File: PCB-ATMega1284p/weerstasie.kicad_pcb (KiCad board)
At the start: 2 copper layers, 35 x 87 mm, 42 parts, among them J1 WIND, J10 Conn_01x01, J11 INT2, J12 I2C, J13 UART, J2 batt -, J3 batt +, J4 RAIN, J5 Conn_01x01, J6 Conn_01x01, J7 Conn_01x01, J8 Conn_01x01, J9 Conn_01x01, SW1 SW_Push, U1 BME280, U2 RFM95, U3 ATMEGA1284P-AU, Y1 8MHz

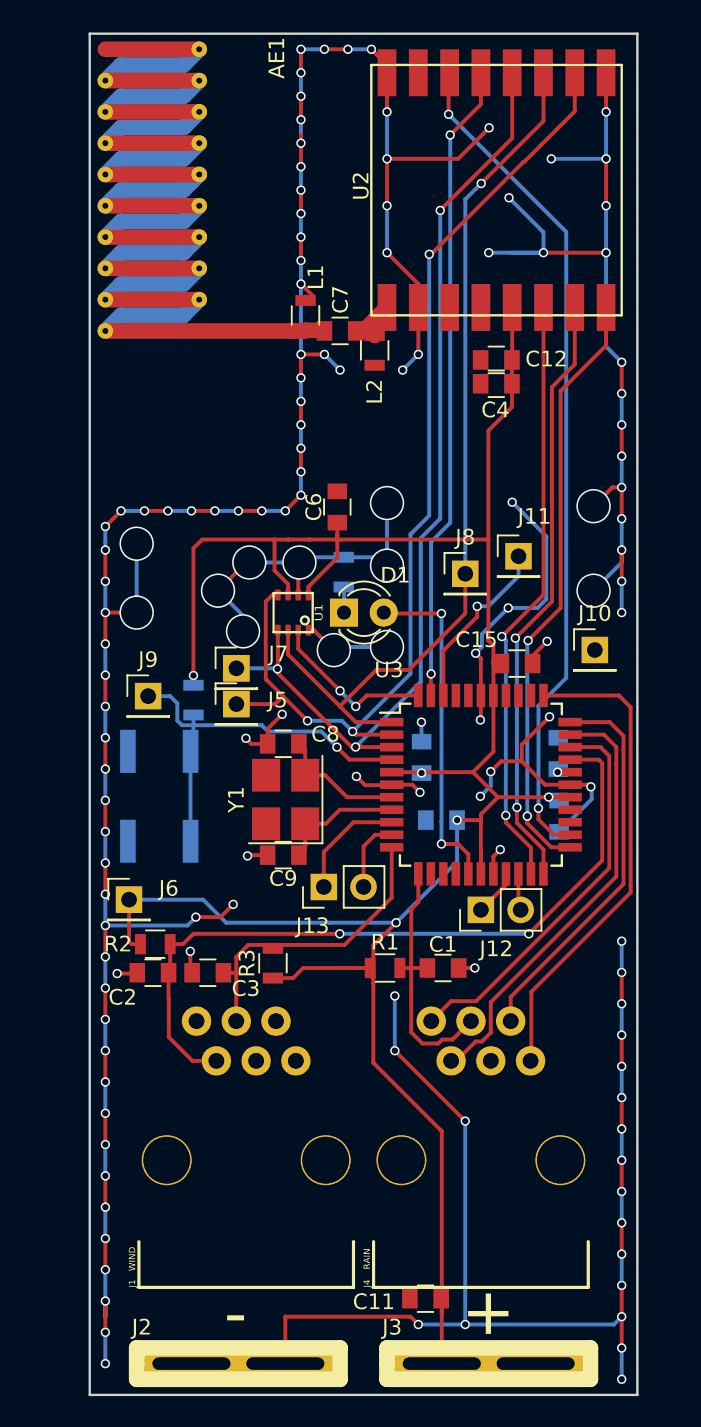
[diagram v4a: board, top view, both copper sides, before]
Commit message: Update to kicad 5 Move rj11's closer together
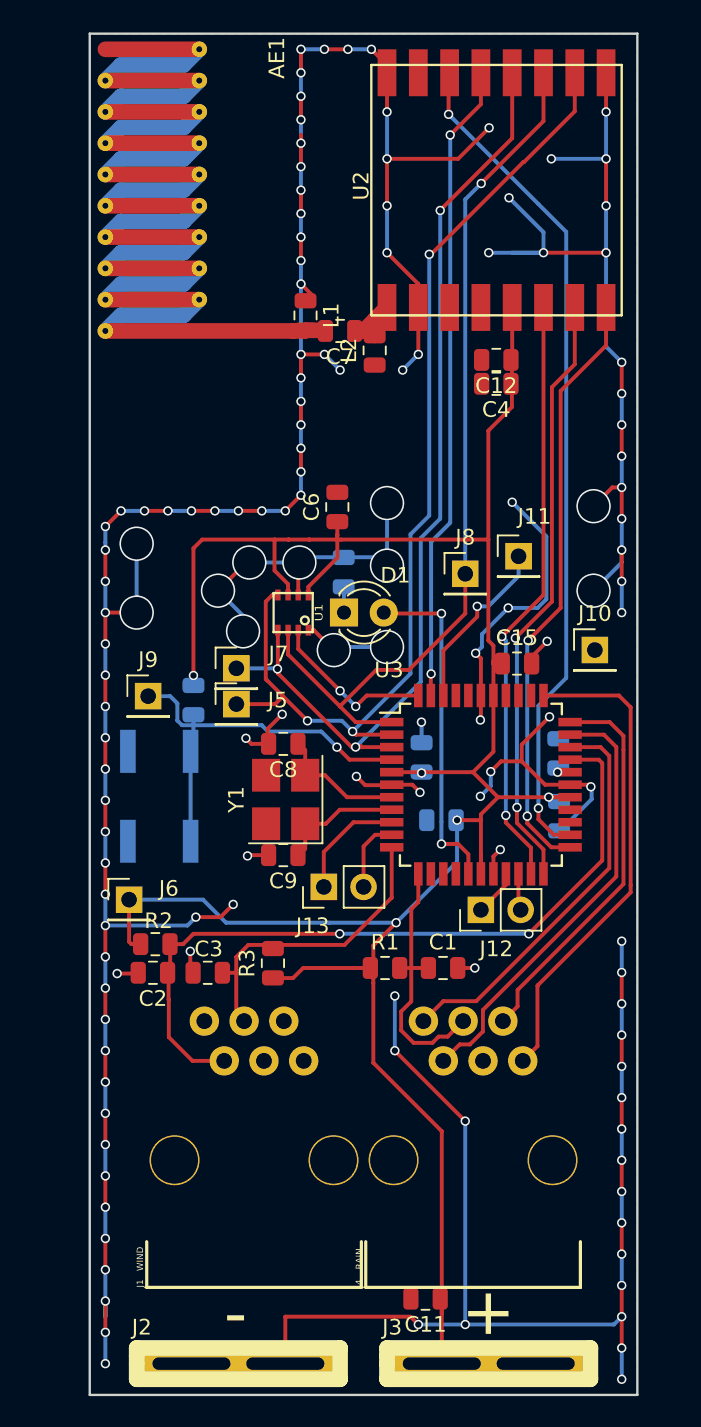
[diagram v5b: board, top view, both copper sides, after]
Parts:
- C1, C10, C11, C12, C13, C14, C15, C2, C3, C4, C5, C6, C7, C8, C9: footprint Capacitors_SMD:C_0805 -> Capacitor_SMD:C_0805_2012Metric
- L1, L2: footprint Inductors_SMD:L_0805 -> Inductor_SMD:L_0805_2012Metric
- R1: value 10k1 -> 10k; footprint Resistors_SMD:R_0805 -> Resistor_SMD:R_0805_2012Metric
- R2: value 10k2 -> 10k; footprint Resistors_SMD:R_0805 -> Resistor_SMD:R_0805_2012Metric
- R3: value 10k3 -> 10k; footprint Resistors_SMD:R_0805 -> Resistor_SMD:R_0805_2012Metric
- R4: footprint Resistors_SMD:R_0805 -> Resistor_SMD:R_0805_2012Metric
- R5: value 200? -> 10k; footprint Resistors_SMD:R_0805 -> Resistor_SMD:R_0805_2012Metric
- moved J1 0.50 mm to (110.5, 118.0)
- moved J4 0.50 mm to (124.5, 118.0)
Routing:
- net /SOLAR_1: track 25.3 -> 25.8 mm

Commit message: Fix RJ11 solder mask. Add v1.4 label. Order from JLC.
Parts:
- C10, C12, C13, C14, C15: value 100nF -> 100n
- C11, C4: value 10uF -> 10u
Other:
- board text added: "IZINTO.cloud"
- board text added: "Weather station v1.4 © 2019"

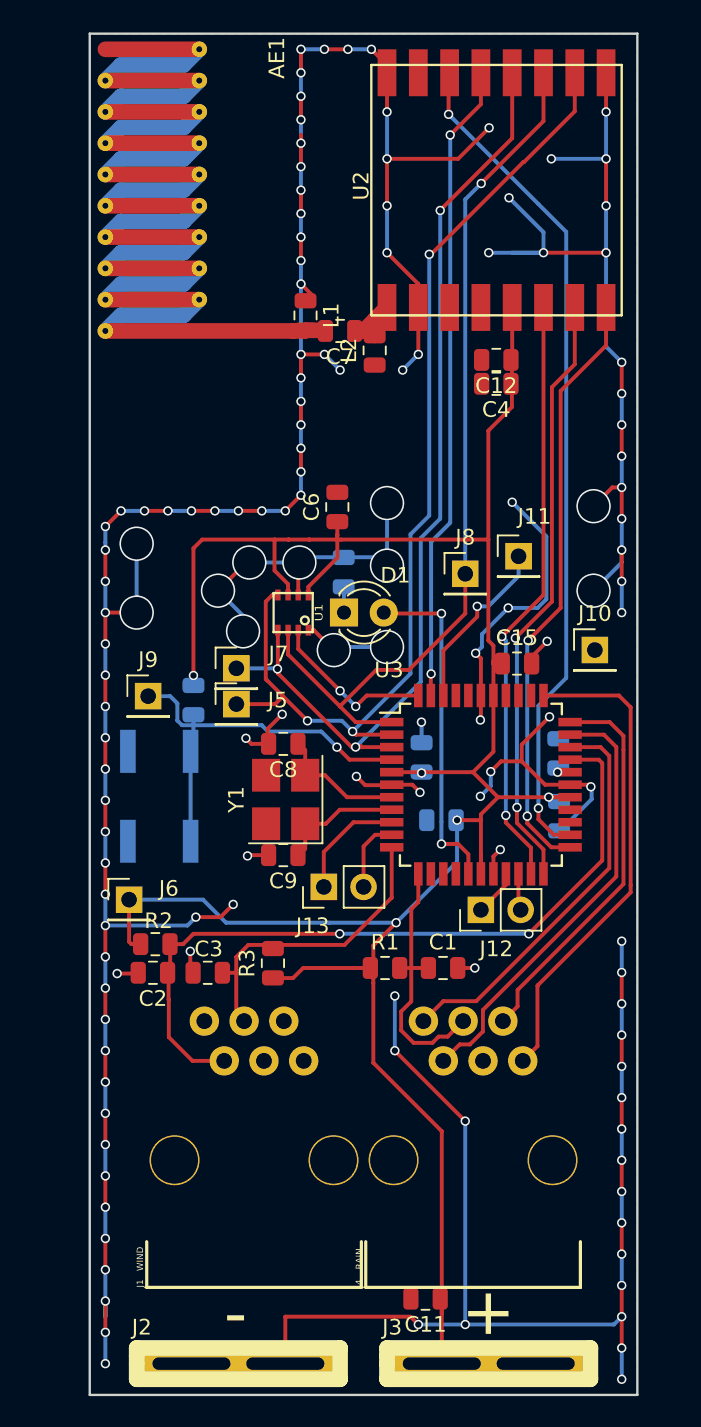
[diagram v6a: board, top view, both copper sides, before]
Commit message: Remove solar connections. Add uart on rain rj12.
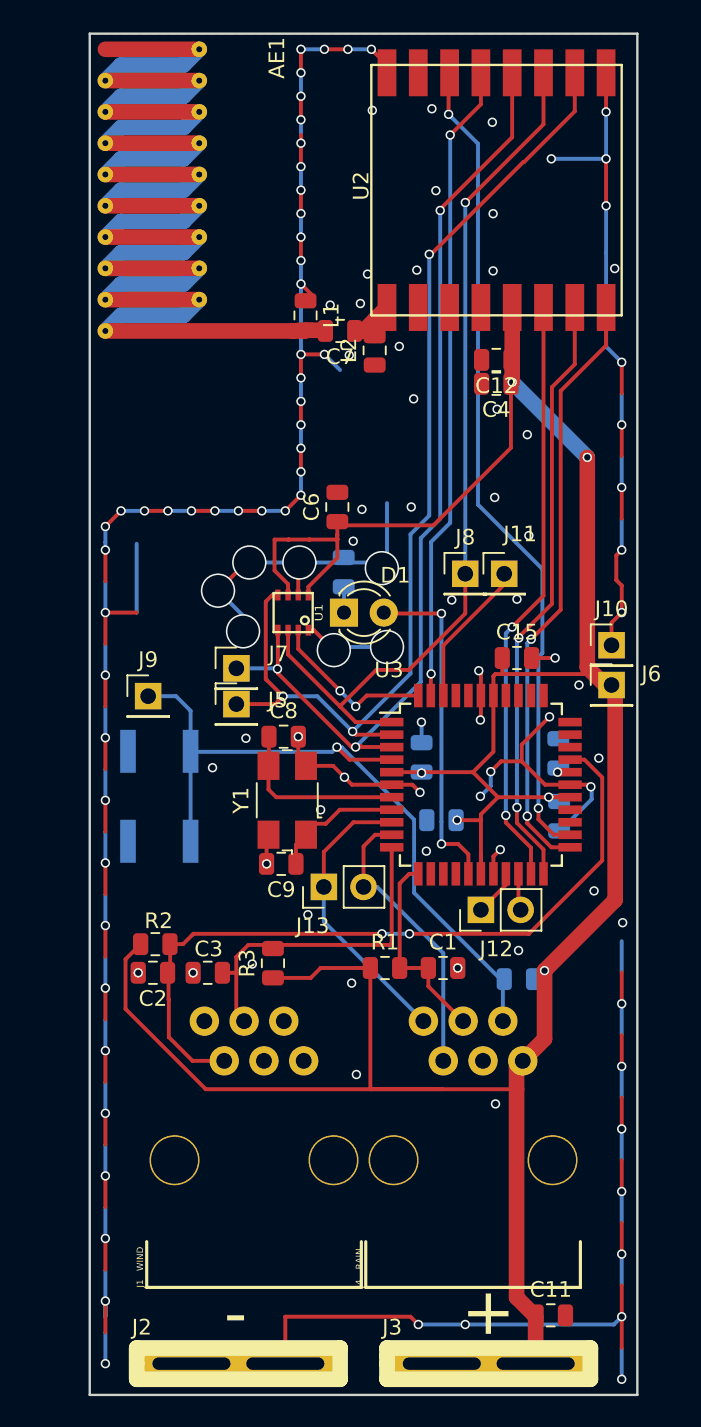
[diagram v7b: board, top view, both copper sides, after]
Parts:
- Y1: value 8MHz -> Crystal_GND24; footprint Crystals:Crystal_SMD_SeikoEpson_FA238V-4pin_3.2x2.5mm_HandSoldering -> Crystal:Crystal_SMD_0603-4Pin_6.0x3.5mm
- moved J6 33.7 mm to (133.3, 87.6)
- moved R4 27.4 mm to (127.4, 106.4), turned to 180 degrees
- moved C11 8.07 mm to (129.5, 127.9), turned to 0 degrees
- moved J11 1.44 mm to (126.5, 80.5)
- moved J10 1.11 mm to (133.3, 85.1)
- moved C9 0.57 mm to (112.2, 99.1)
- moved C8 0.46 mm to (112.4, 90.9), turned to 0 degrees
- moved C15 0.36 mm to (127.3, 85.9)
- moved Y1 0.11 mm to (112.6, 95.0)
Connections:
- J1 pad 1: (no net) -> Net-(J1-Pad1)
- J1 pad 6: (no net) -> Net-(J1-Pad6)
- J13 pad 1: Net-(J13-Pad1) -> /UART_RX
- J13 pad 2: Net-(J13-Pad2) -> /UART_TX
- J4 pad 1: /SOLAR_1 -> /UART_RX
- J4 pad 2: /SOLAR_2 -> /UART_TX
- J4 pad 5: /SOLAR_5 -> /RESET
- J4 pad 6: /SOLAR_6 -> VCC
- U2 pad 11: (no net) -> Net-(U2-Pad11)
- U2 pad 12: (no net) -> Net-(U2-Pad12)
- U2 pad 7: (no net) -> Net-(U2-Pad7)
- U3 pad 10: Net-(J13-Pad2) -> /UART_TX
- U3 pad 13: (no net) -> Net-(U3-Pad13)
- U3 pad 14: (no net) -> Net-(U3-Pad14)
- U3 pad 15: (no net) -> Net-(U3-Pad15)
- U3 pad 25: (no net) -> Net-(U3-Pad25)
- U3 pad 26: (no net) -> Net-(U3-Pad26)
- U3 pad 31: /SOLAR_1 -> Net-(U3-Pad31)
- U3 pad 32: /SOLAR_2 -> Net-(U3-Pad32)
- U3 pad 33: /SOLAR_5 -> Net-(U3-Pad33)
- U3 pad 34: /SOLAR_6 -> Net-(U3-Pad34)
- U3 pad 35: (no net) -> Net-(U3-Pad35)
- U3 pad 36: (no net) -> Net-(U3-Pad36)
- U3 pad 37: (no net) -> Net-(U3-Pad37)
- U3 pad 40: (no net) -> Net-(U3-Pad40)
- U3 pad 41: (no net) -> Net-(U3-Pad41)
- U3 pad 9: Net-(J13-Pad1) -> /UART_RX
- Y1 pad 2: Net-(C8-Pad1) -> GND
- Y1 pad 3: (no net) -> Net-(C8-Pad1)
- Y1 pad 4: (no net) -> GND
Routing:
- net GND: track 366.9 -> 274.9 mm, vias 136 -> 123
- net VCC: track 166.3 -> 200.6 mm, vias 5 -> 6
- net /SOLAR_6: track 31.3 -> 0.00 mm
- net /SOLAR_2: track 28.3 -> 0.00 mm
- net /SOLAR_1: track 25.8 -> 0.00 mm
- net /SOLAR_5: track 25.2 -> 0.00 mm
- net /RESET: track 26.4 -> 47.5 mm
- net /UART_RX: track 0.00 -> 18.6 mm
- net /UART_TX: track 0.00 -> 18.4 mm
- net Net-(J13-Pad1): track 7.36 -> 0.00 mm
- net Net-(J13-Pad2): track 4.70 -> 0.00 mm
- net /RAIN: track 17.1 -> 12.9 mm
- net Net-(C8-Pad1): track 8.28 -> 11.5 mm
- net Net-(J11-Pad1): track 11.3 -> 9.39 mm, vias 1 -> 0
- net /WIND_SPEED: track 20.4 -> 22.1 mm
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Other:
- board text added: "Weather station v1.5 © 2020"
- board text removed: "Weather station v1.4 © 2019"

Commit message: Misol Lora Atmega V1.5 order placed with PCBgogo
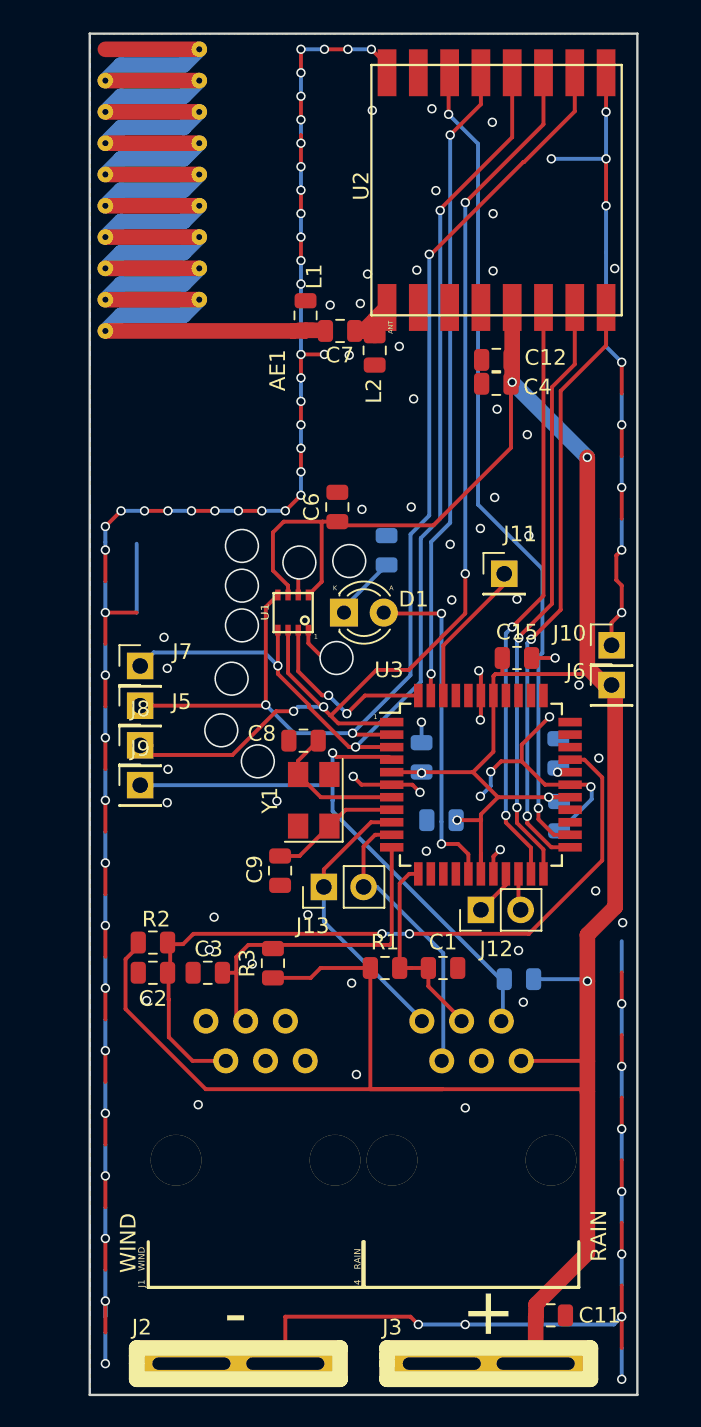
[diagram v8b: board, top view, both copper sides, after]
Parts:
- removed SW1: SW_Push, Buttons_Switches_SMD:SW_SPST_B3SL-1002P
- J1, J4: footprint drawn_by_jpmeijers:SPARKFUN_RJ11-6 -> drawn_by_jpmeijers:TE_Connectivity_5520425-3
- Y1: footprint Crystal:Crystal_SMD_0603-4Pin_6.0x3.5mm -> Crystal:Crystal_SMD_5032-4Pin_5.0x3.2mm
- moved J8 23.5 mm to (103.2, 91.5)
- moved J7 6.15 mm to (103.2, 86.4)
- moved J5 6.15 mm to (103.2, 89.0)
- moved J9 5.71 mm to (103.2, 94.0)
- moved R5 3.08 mm to (119.0, 79.0)
- moved Y1 1.69 mm to (114.3, 95.0)
- moved C8 1.30 mm to (113.7, 91.2), turned to 180 degrees
- moved C9 0.44 mm to (112.2, 99.5), turned to 270 degrees
- moved R2 0.18 mm to (104.0, 104.1)
- moved J1 0.10 mm to (110.6, 118.0)
- moved J4 0.10 mm to (124.4, 118.0)
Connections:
- J1 pad 1: Net-(J1-Pad1) -> (no net)
- J1 pad 6: Net-(J1-Pad6) -> (no net)
- U2 pad 11: Net-(U2-Pad11) -> (no net)
- U2 pad 12: Net-(U2-Pad12) -> (no net)
- U2 pad 7: Net-(U2-Pad7) -> (no net)
- U3 pad 13: Net-(U3-Pad13) -> (no net)
- U3 pad 14: Net-(U3-Pad14) -> (no net)
- U3 pad 15: Net-(U3-Pad15) -> (no net)
- U3 pad 25: Net-(U3-Pad25) -> (no net)
- U3 pad 26: Net-(U3-Pad26) -> (no net)
- U3 pad 31: Net-(U3-Pad31) -> (no net)
- U3 pad 32: Net-(U3-Pad32) -> (no net)
- U3 pad 33: Net-(U3-Pad33) -> (no net)
- U3 pad 34: Net-(U3-Pad34) -> (no net)
- U3 pad 35: Net-(U3-Pad35) -> (no net)
- U3 pad 36: Net-(U3-Pad36) -> (no net)
- U3 pad 37: Net-(U3-Pad37) -> (no net)
- U3 pad 40: Net-(U3-Pad40) -> (no net)
- U3 pad 41: Net-(U3-Pad41) -> (no net)
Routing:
- net GND: track 274.9 -> 242.1 mm, vias 123 -> 128
- net /MOSI: track 57.1 -> 72.8 mm, vias 1 -> 4
- net VCC: track 200.6 -> 211.2 mm
- net /RESET: track 47.5 -> 37.9 mm
- net /SCK: track 63.0 -> 69.4 mm
- net /MISO: track 67.1 -> 72.4 mm
- net Net-(D1-Pad1): track 1.74 -> 4.27 mm
- net Net-(C8-Pad1): track 11.5 -> 9.28 mm
- net /BME_SS: track 10.7 -> 11.9 mm
- net /UART_RX: track 18.6 -> 17.9 mm
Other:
- board text added: "1"
- board text added: "A"
- board text added: "ANT"
- board text added: "K"
- board text added: "LoRa Weather Station v1.5 © 2020"
- board text added: "RAIN"
- board text added: "WIND"
- board text removed: "Weather station v1.5 © 2020"
